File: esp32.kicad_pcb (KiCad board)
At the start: 2 copper layers, 25.4 x 41.8 mm, 23 parts, among them IC1 ESP32-WROVER-E_M213EH6464PH3Q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, J1 Micro_SD_Card_Det, J4 Bus_Connector, U1 MCP2518FDT-H_SL, U2 SN65HVD231, U3 SRV05-4, Y1 XRCGB40M000F4M02R0

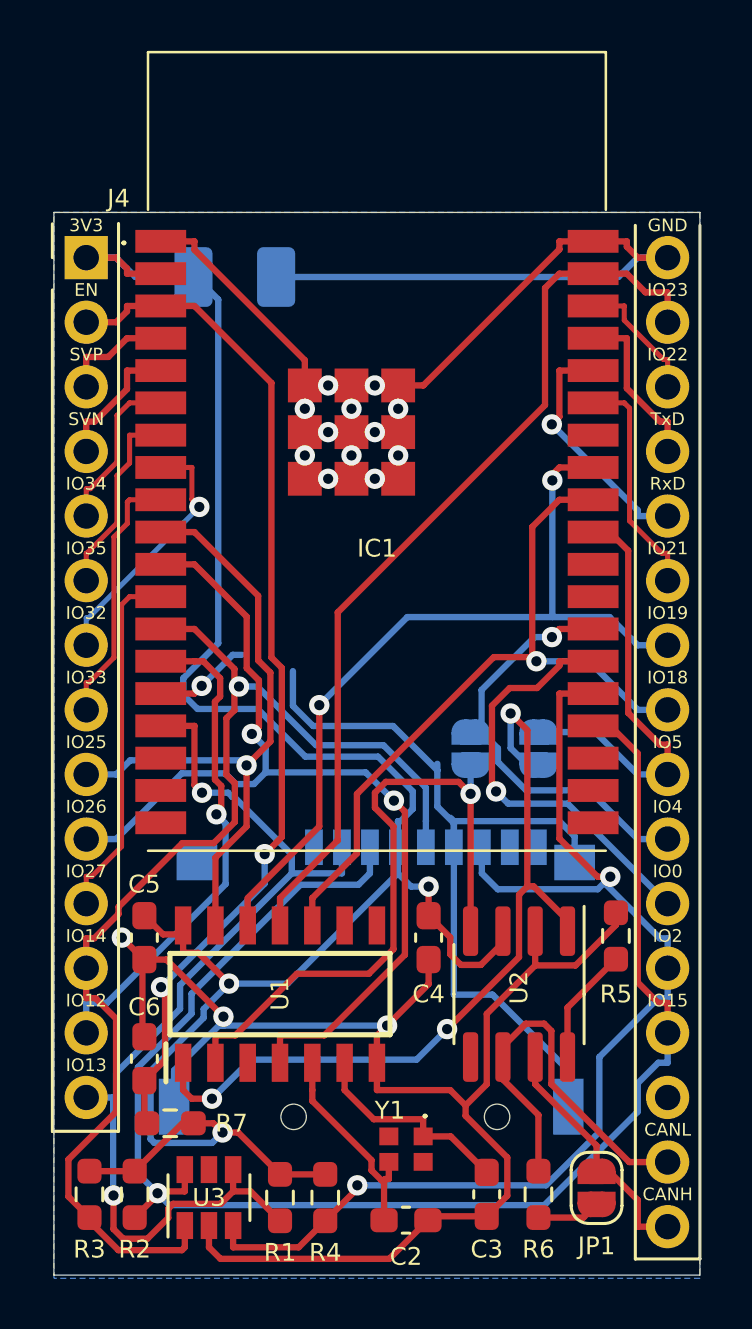
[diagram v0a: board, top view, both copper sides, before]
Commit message: - SN65 RS an GPIO 27 - Quarz Footprint 3225
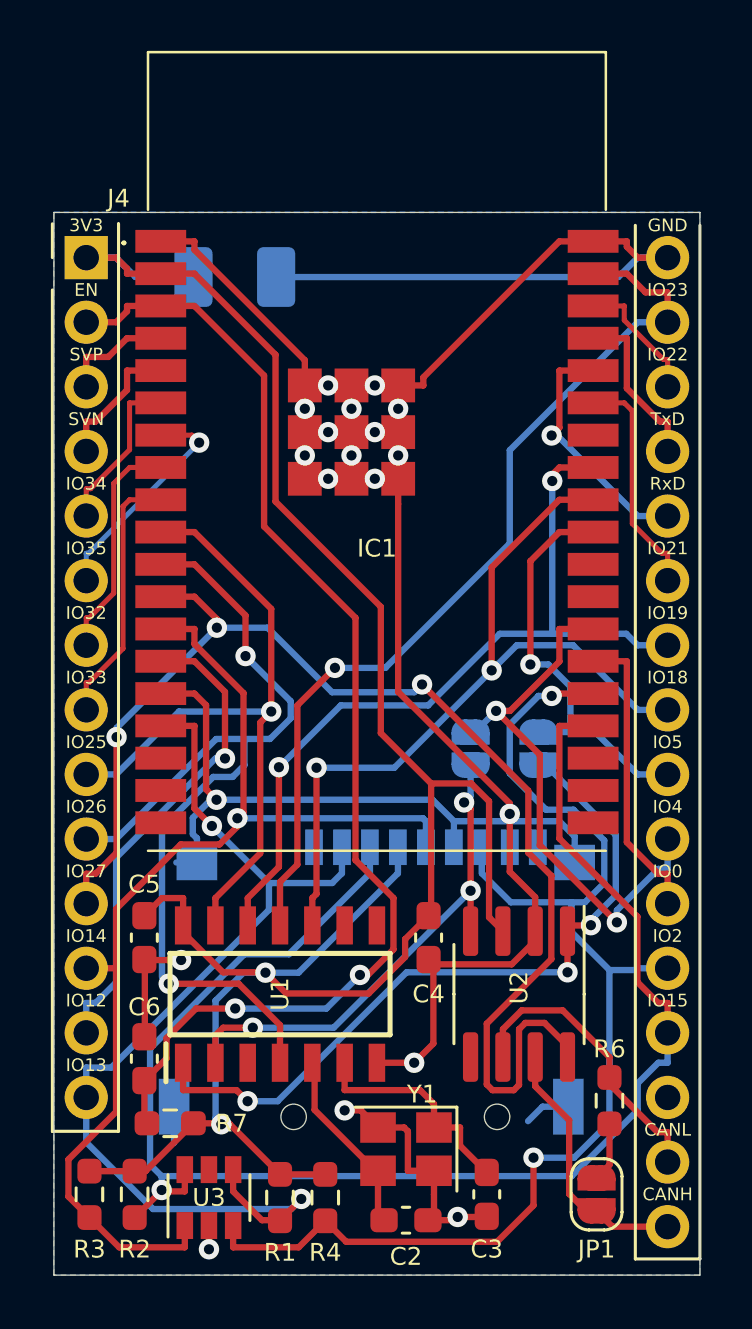
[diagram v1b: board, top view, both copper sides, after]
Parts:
- removed R5: 5k, Resistor_SMD:R_0603_1608Metric_Pad0.98x0.95mm_HandSolder
- Y1: value XRCGB40M000F4M02R0 -> 40MHz; footprint mcp2518:XRCGB40M000F4M02R0 -> Crystal:Crystal_SMD_3225-4Pin_3.2x2.5mm
- moved R6 4.62 mm to (106.9, 99.2)
- moved JP1 0.25 mm to (106.4, 102.9), turned to 90 degrees
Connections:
- IC1 pad 12: Net-(IC1-Pad12) -> SN65_RS
- J4 pad 11: Net-(IC1-Pad12) -> SN65_RS
- U2 pad 8: Net-(R5-Pad1) -> SN65_RS
- Y1 pad 2: Net-(Y1-Pad2) -> GND
- Y1 pad 4: Net-(Y1-Pad4) -> GND
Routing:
- net SN65_RS: track 0.00 -> 50.7 mm, vias 0 -> 3
- net GND: track 147.7 -> 132.9 mm, vias 16 -> 19
- net Net-(IC1-Pad12): track 14.1 -> 0.00 mm
- net EN: track 40.6 -> 47.3 mm
- net RXCAN: track 26.6 -> 20.2 mm, vias 1 -> 3
- net +3V3: track 81.9 -> 87.8 mm, vias 3 -> 2
- net IO0: track 16.8 -> 11.7 mm, vias 1 -> 0
- net IO4: track 16.9 -> 21.8 mm, vias 1 -> 2
- net Net-(R5-Pad1): track 4.64 -> 0.00 mm
- net CANL: track 15.8 -> 11.7 mm
- net SD_DAT0: track 45.7 -> 49.9 mm
- net SD_CLK: track 47.3 -> 44.1 mm
- net MCP_CLK: track 29.2 -> 32.3 mm, vias 1 -> 2
- net TXCAN: track 32.0 -> 29.6 mm
- net MCP_CS: track 25.5 -> 27.3 mm
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
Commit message: Beschriftung zugefügt
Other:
- board text added: "ESP32 CAN V2"
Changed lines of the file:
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@@
   (general
     (thickness 1.6)
-    (drawings 5)
+    (drawings 6)
     (tracks 555)
     (zones 0)
@@
       ))
   )
+  (gr_text "ESP32 CAN V2" (at 97.79 77.47) (layer B.SilkS)
+    (effects (font (size 1 1) (thickness 0.15)) (justify mirror))
+  )
   (gr_text "Closed =\nInt. CAN\nNo MCP2518" (at 104.902 82.042) (layer B.SilkS)
     (effects (font (size 0.7 0.7) (thickness 0.1)) (justify left mirror))
@@
   (gr_line (start 110.49 64.262) (end 110.49 106.045) (layer Edge.Cuts) (width 0.05))
   (gr_line (start 85.09 64.262) (end 110.49 64.262) (layer Edge.Cuts) (width 0.05))
-  (via (at 100.965 103.759) (size 0.8) (drill 0.4) (layers F.Cu B.Cu) (net 23))
   (segment (start 86.36 71.12) (end 86.36 69.9447) (width 0.25) (layer F.Cu) (net 1))
   (segment (start 89.29 69.21) (end 87.9647 69.21) (width 0.25) (layer F.Cu) (net 1))
@@
   (via (at 91.6727 100.1142) (size 0.8) (layers F.Cu B.Cu) (net 22))
   (via (at 93.4075 94.154) (size 0.8) (layers F.Cu B.Cu) (net 22))
+  (via (at 100.965 103.759) (size 0.8) (drill 0.4) (layers F.Cu B.Cu) (net 23))
   (segment (start 98.625 75.7253) (end 98.625 83.1093) (width 0.25) (layer F.Cu) (net 23))
   (segment (start 98.625 83.1093) (end 103.0128 87.4971) (width 0.25) (layer F.Cu) (net 23))
